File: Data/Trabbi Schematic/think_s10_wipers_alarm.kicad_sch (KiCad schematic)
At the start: 7 parts, among them K1 Wiper Relay R1, K2 Tailgate Release Relay R13, M1 Wiper Motor (E19), M2 Washer Pump (E10), SW1 Wiper Switch (C26), U1 Alarm Control Unit (P4)

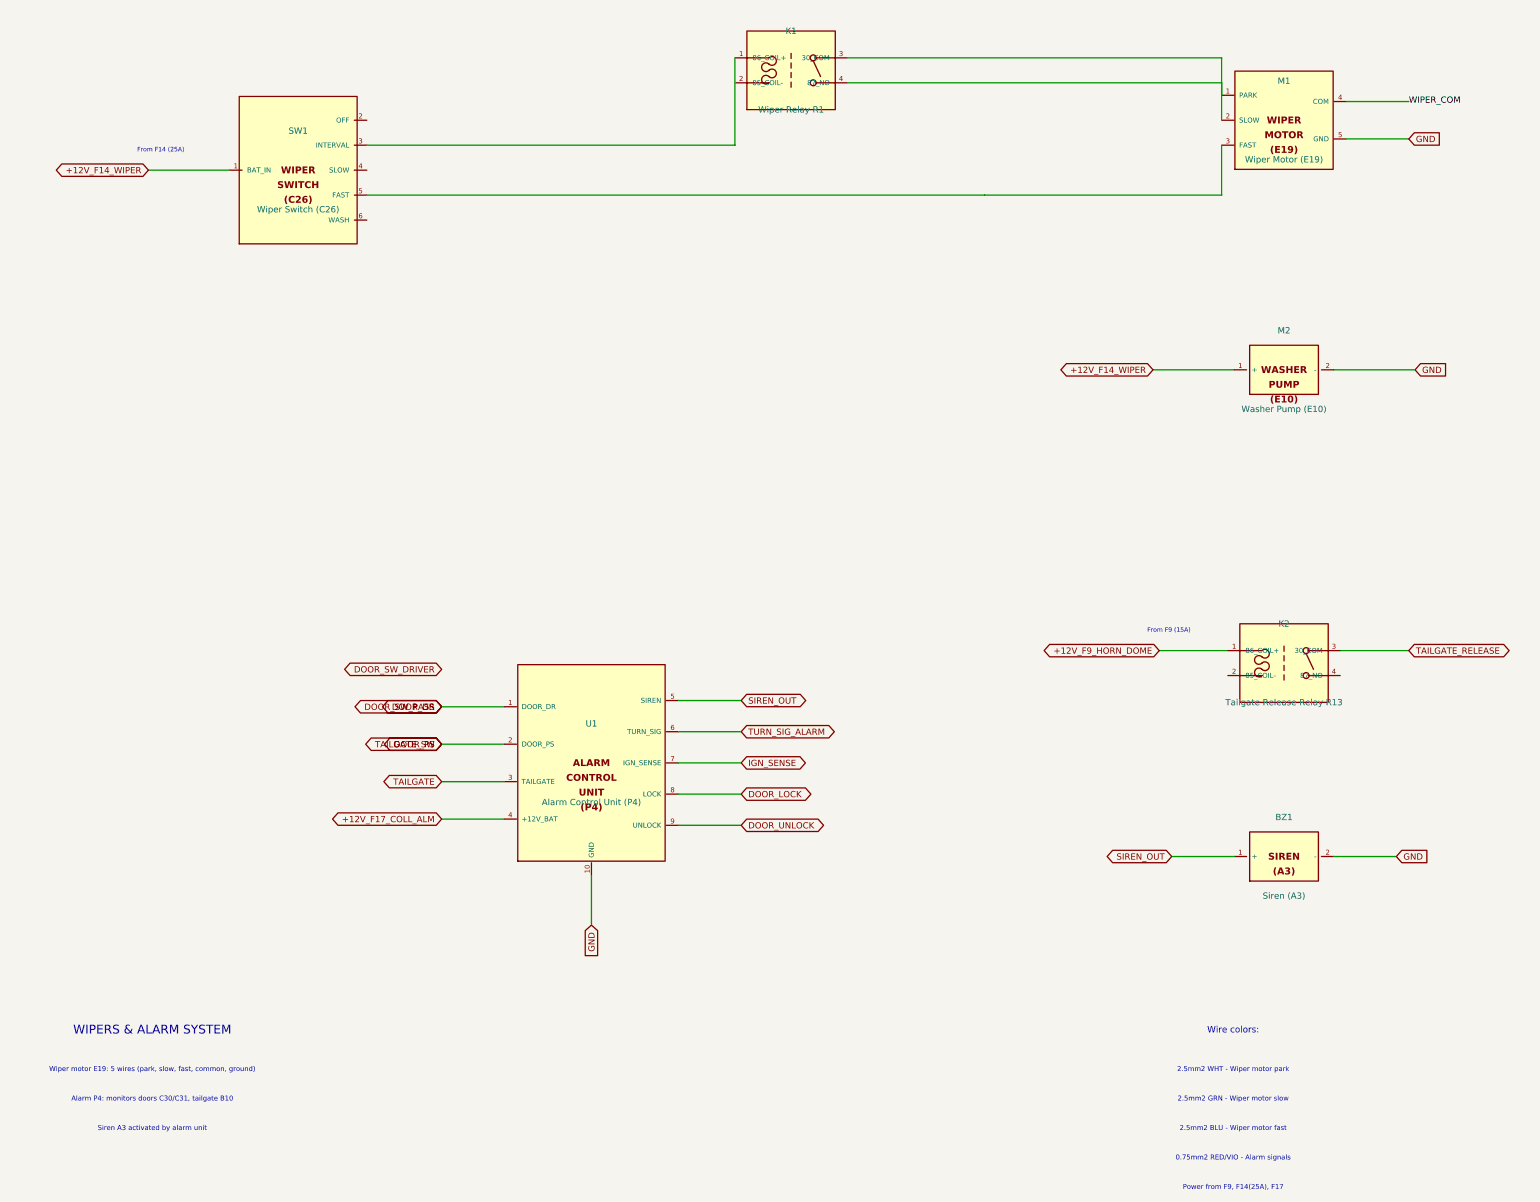
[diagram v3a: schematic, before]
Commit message: Fix label/text positioning: Ref/Value outside body, hide pin numbers
- Reference placed above body edge, Value below (dynamic based on
  symbol height) — no longer overlapping body text
- Pin numbers hidden (clutter, not useful in schematic view)
- Pin name font reduced from 1.016mm to 0.762mm (less overlap)
- Pin length increased from 2.54mm to 3.81mm (more room for pin names
  between body edge and endpoint)
- Store symbol dimensions in _sym_dims for dynamic property placement

Co-Authored-By: Claude Opus 4.6 <noreply@anthropic.com>
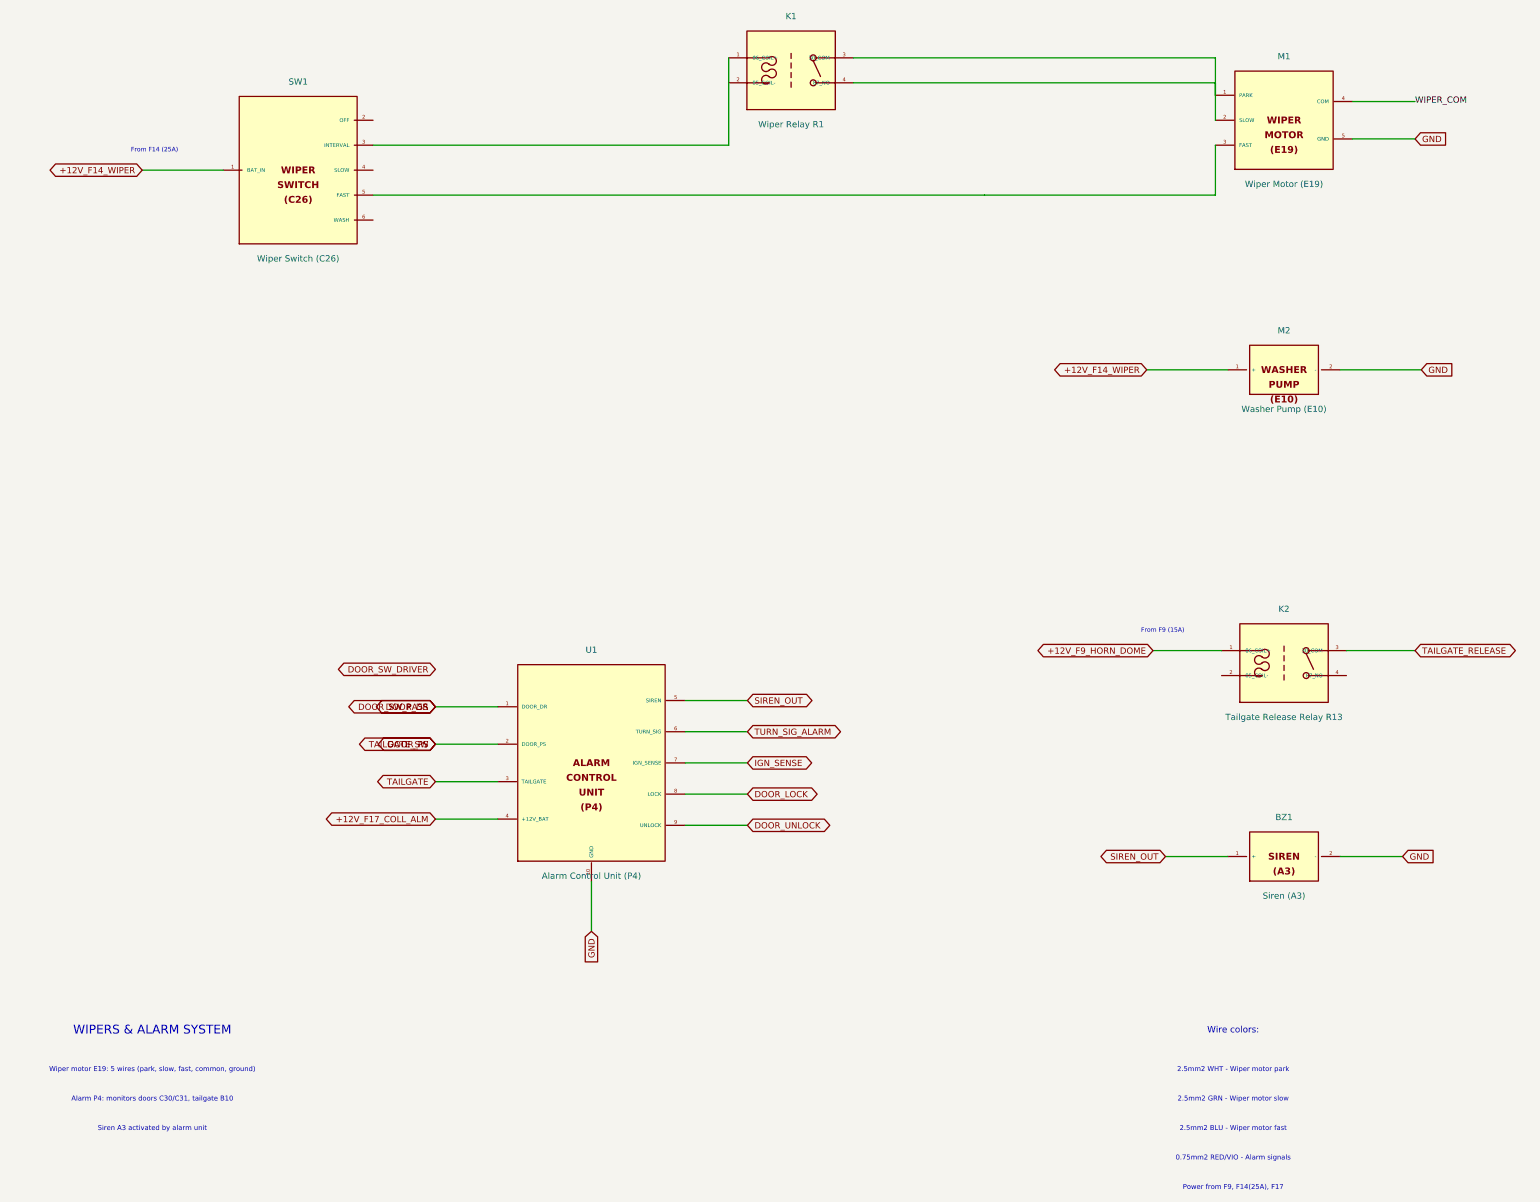
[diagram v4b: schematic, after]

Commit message: Add cross-sheet reference annotations to global labels
- Track all global label positions per sheet during build
- After building all sheets, annotate each global label with
  "→S01,S03,..." text showing which other sheets share the net
- 60 cross-sheet nets identified and annotated
- Two-pass build: 1) build all sheets 2) add cross-refs + save
- Text placed near label in 0.8mm font, offset to avoid overlap

Co-Authored-By: Claude Opus 4.6 <noreply@anthropic.com>
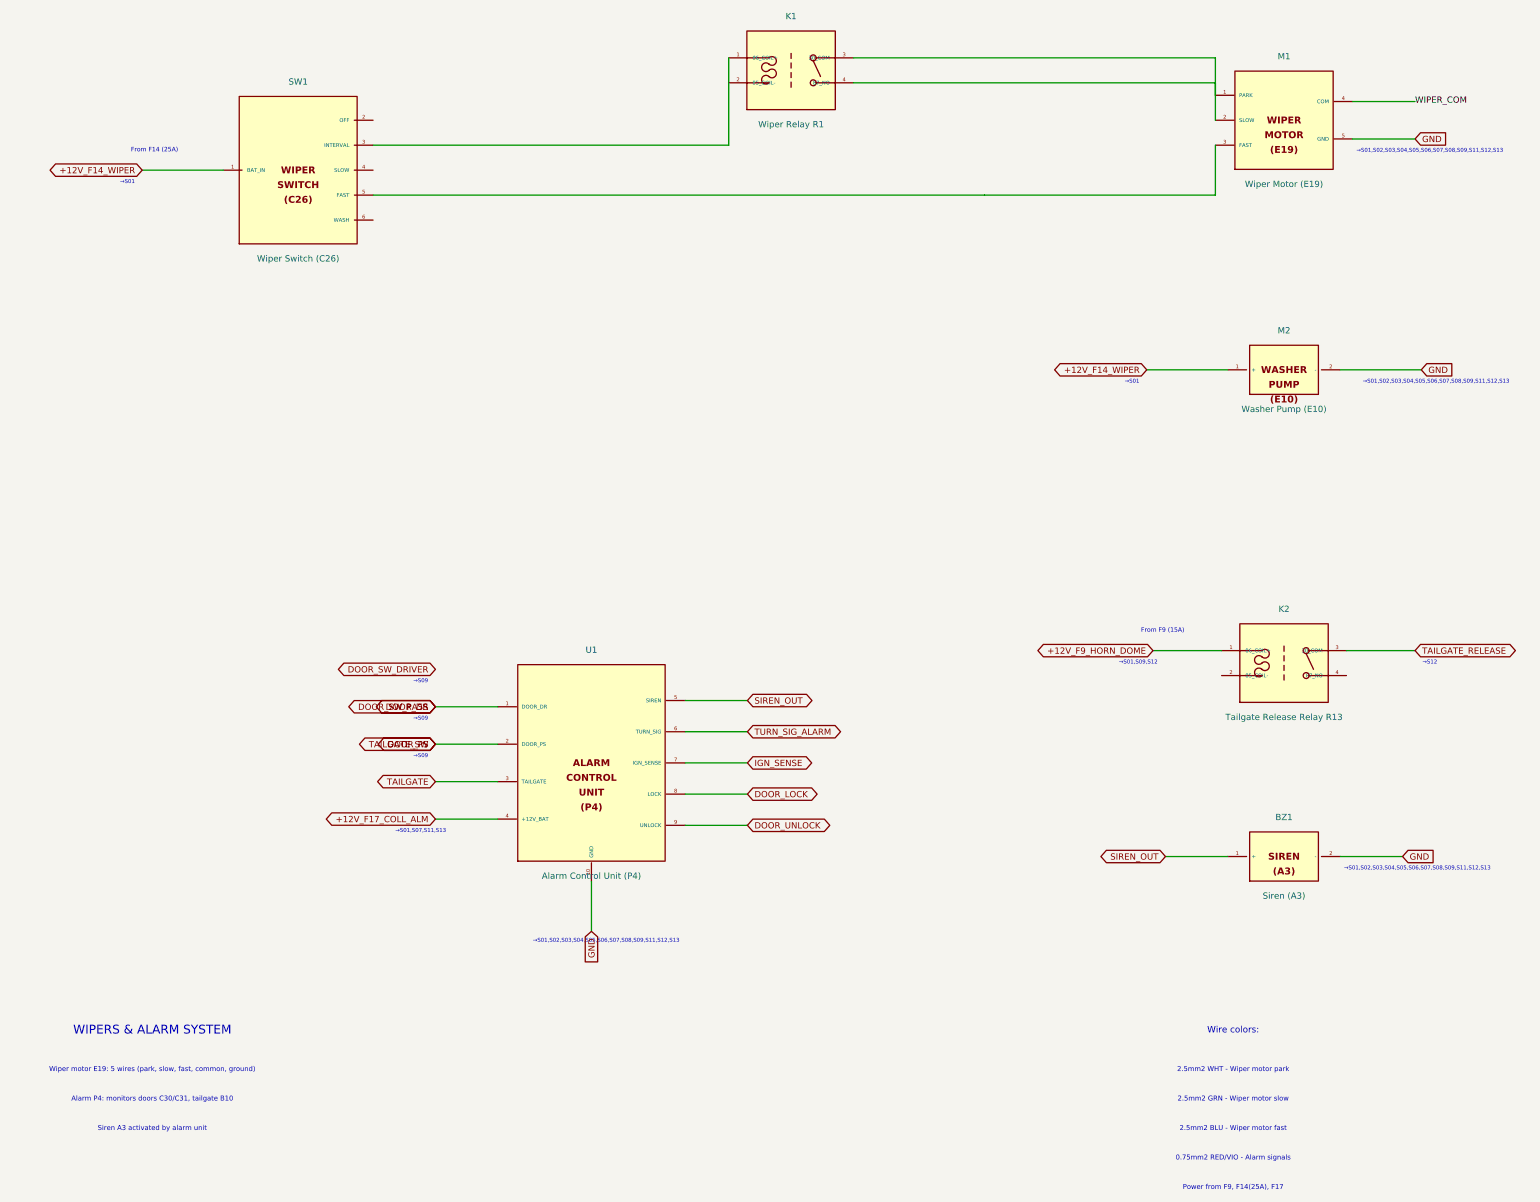
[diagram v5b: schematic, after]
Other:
- note added: "→S01"
- note added: "→S01,S02,S03,S04,S05,S06,S07,S08,S09,S11,S12,S13"
- note added: "→S01,S07,S11,S13"
- note added: "→S01,S09,S12"
- note added: "→S09"
- note added: "→S12"
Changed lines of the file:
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@@
     (effects (font (size 1.000 1.000)))
+  )
+  (text "→S01" (at 24.940 72.350 0)
+    (effects (font (size 0.800 0.800)))
+  )
+  (text "→S01" (at 229.410 112.990 0)
+    (effects (font (size 0.800 0.800)))
+  )
+  (text "→S01,S02,S03,S04,S05,S06,S07,S08,S09,S11,S12,S13" (at 290.020 66.000 0)
+    (effects (font (size 0.800 0.800)))
+  )
+  (text "→S01,S02,S03,S04,S05,S06,S07,S08,S09,S11,S12,S13" (at 291.290 112.990 0)
+    (effects (font (size 0.800 0.800)))
+  )
+  (text "→S01,S02,S03,S04,S05,S06,S07,S08,S09,S11,S12,S13" (at 122.380 226.790 0)
+    (effects (font (size 0.800 0.800)))
+  )
+  (text "→S01,S02,S03,S04,S05,S06,S07,S08,S09,S11,S12,S13" (at 287.480 212.050 0)
+    (effects (font (size 0.800 0.800)))
+  )
+  (text "→S01,S07,S11,S13" (at 84.630 204.430 0)
+    (effects (font (size 0.800 0.800)))
+  )
+  (text "→S01,S09,S12" (at 230.680 170.140 0)
+    (effects (font (size 0.800 0.800)))
+  )
+  (text "→S12" (at 290.020 170.140 0)
+    (effects (font (size 0.800 0.800)))
+  )
+  (text "→S09" (at 84.630 173.950 0)
+    (effects (font (size 0.800 0.800)))
+  )
+  (text "→S09" (at 84.630 181.570 0)
+    (effects (font (size 0.800 0.800)))
+  )
+  (text "→S09" (at 84.630 189.190 0)
+    (effects (font (size 0.800 0.800)))
   )
   (symbol_instances)

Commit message: Fix label text justification for KiCad 9
Add (justify left) to all label and global_label effects.
KiCad 9 requires explicit text justification — without it,
label text is mispositioned relative to the label shape.

Co-Authored-By: Claude Opus 4.6 <noreply@anthropic.com>
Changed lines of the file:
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@@
   )
   (global_label "+12V_F14_WIPER" (shape bidirectional) (at 27.940 69.850 180)
-    (effects (font (size 1.27 1.27)))
+    (effects (font (size 1.27 1.27)) (justify left))
     (property "Intersheetrefs" "${INTERSHEET_REFS}" (at 27.940 69.850 0)
       (effects (font (size 1.27 1.27)) hide)
@@
   )
   (global_label "GND" (shape input) (at 287.020 63.500 0)
-    (effects (font (size 1.27 1.27)))
+    (effects (font (size 1.27 1.27)) (justify left))
     (property "Intersheetrefs" "${INTERSHEET_REFS}" (at 287.020 63.500 0)
       (effects (font (size 1.27 1.27)) hide)
@@
   )
   (label "WIPER_COM" (at 287.020 55.880 0)
-    (effects (font (size 1.27 1.27)))
+    (effects (font (size 1.27 1.27)) (justify left))
   )
   (wire (pts (xy 248.920 110.490) (xy 232.410 110.490))
@@
   )
   (global_label "+12V_F14_WIPER" (shape bidirectional) (at 232.410 110.490 180)
-    (effects (font (size 1.27 1.27)))
+    (effects (font (size 1.27 1.27)) (justify left))
     (property "Intersheetrefs" "${INTERSHEET_REFS}" (at 232.410 110.490 0)
       (effects (font (size 1.27 1.27)) hide)
@@
   )
   (global_label "GND" (shape input) (at 288.290 110.490 0)
-    (effects (font (size 1.27 1.27)))
+    (effects (font (size 1.27 1.27)) (justify left))
     (property "Intersheetrefs" "${INTERSHEET_REFS}" (at 288.290 110.490 0)
       (effects (font (size 1.27 1.27)) hide)
@@
   )
   (global_label "DOOR_DR" (shape bidirectional) (at 87.630 179.070 180)
-    (effects (font (size 1.27 1.27)))
+    (effects (font (size 1.27 1.27)) (justify left))
     (property "Intersheetrefs" "${INTERSHEET_REFS}" (at 87.630 179.070 0)
       (effects (font (size 1.27 1.27)) hide)
@@
   )
   (global_label "DOOR_PS" (shape bidirectional) (at 87.630 186.690 180)
-    (effects (font (size 1.27 1.27)))
+    (effects (font (size 1.27 1.27)) (justify left))
     (property "Intersheetrefs" "${INTERSHEET_REFS}" (at 87.630 186.690 0)
       (effects (font (size 1.27 1.27)) hide)
@@
   )
   (global_label "TAILGATE" (shape bidirectional) (at 87.630 194.310 180)
-    (effects (font (size 1.27 1.27)))
+    (effects (font (size 1.27 1.27)) (justify left))
     (property "Intersheetrefs" "${INTERSHEET_REFS}" (at 87.630 194.310 0)
       (effects (font (size 1.27 1.27)) hide)
@@
   )
   (global_label "+12V_F17_COLL_ALM" (shape bidirectional) (at 87.630 201.930 180)
-    (effects (font (size 1.27 1.27)))
+    (effects (font (size 1.27 1.27)) (justify left))
     (property "Intersheetrefs" "${INTERSHEET_REFS}" (at 87.630 201.930 0)
       (effects (font (size 1.27 1.27)) hide)
@@
   )
   (global_label "SIREN_OUT" (shape bidirectional) (at 151.130 177.800 0)
-    (effects (font (size 1.27 1.27)))
+    (effects (font (size 1.27 1.27)) (justify left))
     (property "Intersheetrefs" "${INTERSHEET_REFS}" (at 151.130 177.800 0)
       (effects (font (size 1.27 1.27)) hide)
@@
   )
   (global_label "TURN_SIG_ALARM" (shape bidirectional) (at 151.130 184.150 0)
-    (effects (font (size 1.27 1.27)))
+    (effects (font (size 1.27 1.27)) (justify left))
     (property "Intersheetrefs" "${INTERSHEET_REFS}" (at 151.130 184.150 0)
       (effects (font (size 1.27 1.27)) hide)
@@
   )
   (global_label "IGN_SENSE" (shape bidirectional) (at 151.130 190.500 0)
-    (effects (font (size 1.27 1.27)))
+    (effects (font (size 1.27 1.27)) (justify left))
     (property "Intersheetrefs" "${INTERSHEET_REFS}" (at 151.130 190.500 0)
       (effects (font (size 1.27 1.27)) hide)
@@
   )
   (global_label "DOOR_LOCK" (shape bidirectional) (at 151.130 196.850 0)
-    (effects (font (size 1.27 1.27)))
+    (effects (font (size 1.27 1.27)) (justify left))
     (property "Intersheetrefs" "${INTERSHEET_REFS}" (at 151.130 196.850 0)
       (effects (font (size 1.27 1.27)) hide)
@@
   )
   (global_label "DOOR_UNLOCK" (shape bidirectional) (at 151.130 203.200 0)
-    (effects (font (size 1.27 1.27)))
+    (effects (font (size 1.27 1.27)) (justify left))
     (property "Intersheetrefs" "${INTERSHEET_REFS}" (at 151.130 203.200 0)
       (effects (font (size 1.27 1.27)) hide)
@@
   )
   (global_label "GND" (shape input) (at 119.380 224.790 270)
-    (effects (font (size 1.27 1.27)))
+    (effects (font (size 1.27 1.27)) (justify left))
     (property "Intersheetrefs" "${INTERSHEET_REFS}" (at 119.380 224.790 0)
       (effects (font (size 1.27 1.27)) hide)
@@
   )
   (global_label "SIREN_OUT" (shape bidirectional) (at 236.220 209.550 180)
-    (effects (font (size 1.27 1.27)))
+    (effects (font (size 1.27 1.27)) (justify left))
     (property "Intersheetrefs" "${INTERSHEET_REFS}" (at 236.220 209.550 0)
       (effects (font (size 1.27 1.27)) hide)
@@
   )
   (global_label "GND" (shape input) (at 284.480 209.550 0)
-    (effects (font (size 1.27 1.27)))
+    (effects (font (size 1.27 1.27)) (justify left))
     (property "Intersheetrefs" "${INTERSHEET_REFS}" (at 284.480 209.550 0)
       (effects (font (size 1.27 1.27)) hide)
@@
   )
   (global_label "+12V_F9_HORN_DOME" (shape bidirectional) (at 233.680 167.640 180)
-    (effects (font (size 1.27 1.27)))
+    (effects (font (size 1.27 1.27)) (justify left))
     (property "Intersheetrefs" "${INTERSHEET_REFS}" (at 233.680 167.640 0)
       (effects (font (size 1.27 1.27)) hide)
@@
   )
   (global_label "TAILGATE_RELEASE" (shape bidirectional) (at 287.020 167.640 0)
-    (effects (font (size 1.27 1.27)))
+    (effects (font (size 1.27 1.27)) (justify left))
     (property "Intersheetrefs" "${INTERSHEET_REFS}" (at 287.020 167.640 0)
       (effects (font (size 1.27 1.27)) hide)
@@
   )
   (global_label "DOOR_SW_DRIVER" (shape bidirectional) (at 87.630 171.450 180)
-    (effects (font (size 1.27 1.27)))
+    (effects (font (size 1.27 1.27)) (justify left))
     (property "Intersheetrefs" "${INTERSHEET_REFS}" (at 87.630 171.450 0)
       (effects (font (size 1.27 1.27)) hide)
@@
   )
   (global_label "DOOR_SW_PASS" (shape bidirectional) (at 87.630 179.070 180)
-    (effects (font (size 1.27 1.27)))
+    (effects (font (size 1.27 1.27)) (justify left))
     (property "Intersheetrefs" "${INTERSHEET_REFS}" (at 87.630 179.070 0)
       (effects (font (size 1.27 1.27)) hide)
@@
   )
   (global_label "TAILGATE_SW" (shape bidirectional) (at 87.630 186.690 180)
-    (effects (font (size 1.27 1.27)))
+    (effects (font (size 1.27 1.27)) (justify left))
     (property "Intersheetrefs" "${INTERSHEET_REFS}" (at 87.630 186.690 0)
       (effects (font (size 1.27 1.27)) hide)
